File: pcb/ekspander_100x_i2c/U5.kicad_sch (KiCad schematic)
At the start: 12 parts, among them J12 DG127A-5.08-06P-14-00AH, J13 DG127A-5.08-06P-14-00AH, J14 DG127A-5.08-06P-14-00AH, U26 LTV-847, U27 ITS716G, U28 ITS716G, U29 LTV-847, U5 MCP23017_SP

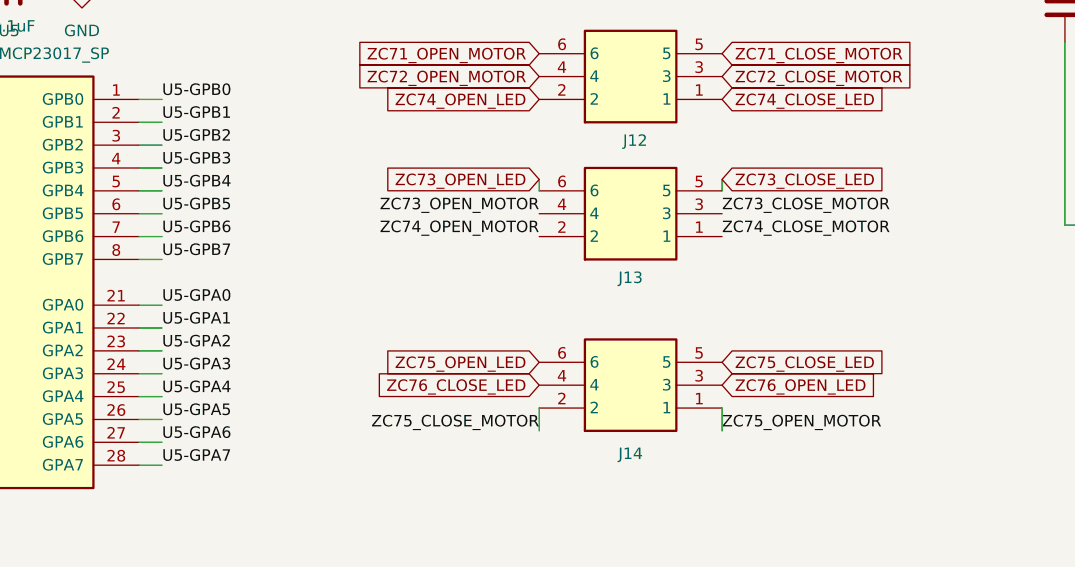
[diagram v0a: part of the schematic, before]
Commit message: Ekspander 100x - finish J
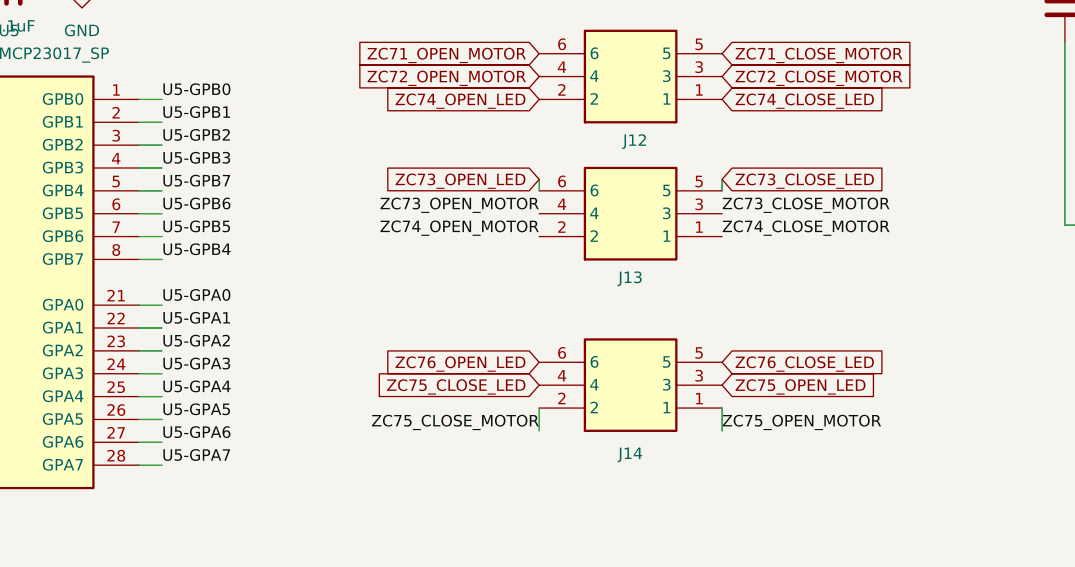
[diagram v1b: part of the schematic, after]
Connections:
- net U5-GPB4: now also U5.8 (GPB7); no longer U5.5 (GPB4)
- net U5-GPB5: now also U5.7 (GPB6); no longer U5.6 (GPB5)
- net U5-GPB6: now also U5.6 (GPB5); no longer U5.7 (GPB6)
- net U5-GPB7: now also U5.5 (GPB4); no longer U5.8 (GPB7)
- net ZC75_CLOSE_LED: now also J14.4; no longer J14.5
- net ZC75_OPEN_LED: now also J14.3; no longer J14.6
- net ZC76_CLOSE_LED: now also J14.5; no longer J14.4
- net ZC76_OPEN_LED: now also J14.6; no longer J14.3
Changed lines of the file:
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@@
 	)
 	(label "U5-GPB5"
-		(at 69.85 50.8 0)
-		(effects
-			(font
-				(size 1.27 1.27)
-			)
-			(justify left bottom)
-		)
-		(property "Netclass" "GPIO"
-			(at 79.756 50.8 0)
+		(at 69.85 53.34 0)
+		(effects
+			(font
+				(size 1.27 1.27)
+			)
+			(justify left bottom)
+		)
+		(property "Netclass" "GPIO"
+			(at 79.756 53.34 0)
 			(effects
 				(font
@@
 	)
 	(label "U5-GPB7"
-		(at 69.85 55.88 0)
-		(effects
-			(font
-				(size 1.27 1.27)
-			)
-			(justify left bottom)
-		)
-		(property "Netclass" "GPIO"
-			(at 79.756 55.88 0)
+		(at 69.85 48.26 0)
+		(effects
+			(font
+				(size 1.27 1.27)
+			)
+			(justify left bottom)
+		)
+		(property "Netclass" "GPIO"
+			(at 79.756 48.26 0)
 			(effects
 				(font
@@
 	)
 	(label "U5-GPB4"
-		(at 69.85 48.26 0)
-		(effects
-			(font
-				(size 1.27 1.27)
-			)
-			(justify left bottom)
-		)
-		(property "Netclass" "GPIO"
-			(at 80.01 48.26 0)
+		(at 69.85 55.88 0)
+		(effects
+			(font
+				(size 1.27 1.27)
+			)
+			(justify left bottom)
+		)
+		(property "Netclass" "GPIO"
+			(at 80.01 55.88 0)
 			(effects
 				(font
@@
 	)
 	(label "U5-GPB6"
-		(at 69.85 53.34 0)
-		(effects
-			(font
-				(size 1.27 1.27)
-			)
-			(justify left bottom)
-		)
-		(property "Netclass" "GPIO"
-			(at 79.756 53.34 0)
+		(at 69.85 50.8 0)
+		(effects
+			(font
+				(size 1.27 1.27)
+			)
+			(justify left bottom)
+		)
+		(property "Netclass" "GPIO"
+			(at 79.756 50.8 0)
 			(effects
 				(font
@@
 	(global_label "ZC76_CLOSE_LED"
 		(shape input)
-		(at 111.76 69.85 180)
-		(fields_autoplaced yes)
-		(effects
-			(font
-				(size 1.27 1.27)
-			)
-			(justify right)
-		)
-		(property "Intersheetrefs" "${INTERSHEET_REFS}"
-			(at 92.5069 69.85 0)
-			(effects
-				(font
-					(size 1.27 1.27)
-				)
-				(justify right)
+		(at 132.08 67.31 0)
+		(fields_autoplaced yes)
+		(effects
+			(font
+				(size 1.27 1.27)
+			)
+			(justify left)
+		)
+		(property "Intersheetrefs" "${INTERSHEET_REFS}"
+			(at 151.3331 67.31 0)
+			(effects
+				(font
+					(size 1.27 1.27)
+				)
+				(justify left)
 				(hide yes)
 			)
@@
 	(global_label "ZC75_OPEN_LED"
 		(shape input)
-		(at 111.76 67.31 180)
-		(fields_autoplaced yes)
-		(effects
-			(font
-				(size 1.27 1.27)
-			)
-			(justify right)
-		)
-		(property "Intersheetrefs" "${INTERSHEET_REFS}"
-			(at 93.414 67.31 0)
-			(effects
-				(font
-					(size 1.27 1.27)
-				)
-				(justify right)
+		(at 132.08 69.85 0)
+		(fields_autoplaced yes)
+		(effects
+			(font
+				(size 1.27 1.27)
+			)
+			(justify left)
+		)
+		(property "Intersheetrefs" "${INTERSHEET_REFS}"
+			(at 150.426 69.85 0)
+			(effects
+				(font
+					(size 1.27 1.27)
+				)
+				(justify left)
 				(hide yes)
 			)
@@
 	(global_label "ZC75_CLOSE_LED"
 		(shape input)
-		(at 132.08 67.31 0)
-		(fields_autoplaced yes)
-		(effects
-			(font
-				(size 1.27 1.27)
-			)
-			(justify left)
-		)
-		(property "Intersheetrefs" "${INTERSHEET_REFS}"
-			(at 151.3331 67.31 0)
-			(effects
-				(font
-					(size 1.27 1.27)
-				)
-				(justify left)
+		(at 111.76 69.85 180)
+		(fields_autoplaced yes)
+		(effects
+			(font
+				(size 1.27 1.27)
+			)
+			(justify right)
+		)
+		(property "Intersheetrefs" "${INTERSHEET_REFS}"
+			(at 92.5069 69.85 0)
+			(effects
+				(font
+					(size 1.27 1.27)
+				)
+				(justify right)
 				(hide yes)
 			)
@@
 	(global_label "ZC76_OPEN_LED"
 		(shape input)
-		(at 132.08 69.85 0)
-		(fields_autoplaced yes)
-		(effects
-			(font
-				(size 1.27 1.27)
-			)
-			(justify left)
-		)
-		(property "Intersheetrefs" "${INTERSHEET_REFS}"
-			(at 150.426 69.85 0)
-			(effects
-				(font
-					(size 1.27 1.27)
-				)
-				(justify left)
-				(hide yes)
-			)
+		(at 111.76 67.31 180)
+		(fields_autoplaced yes)
+		(effects
+			(font
+				(size 1.27 1.27)
+			)
+			(justify right)
+		)
+		(property "Intersheetrefs" "${INTERSHEET_REFS}"
+			(at 93.414 67.31 0)
+			(effects
+				(font
+					(size 1.27 1.27)
+				)
+				(justify right)
+				(hide yes)
+			)

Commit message: Tech Explorations
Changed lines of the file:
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@@
 		)
 		(property "Value" "+3V3"
-			(at 44.704 21.59 0)
+			(at 48.006 18.034 0)
 			(effects
 				(font
@@
 		(on_board yes)
 		(dnp no)
-		(fields_autoplaced yes)
 		(property "Reference" "R6"
-			(at 43.18 21.59 90)
+			(at 40.132 21.336 90)
 			(effects
 				(font
@@
 		(on_board yes)
 		(dnp no)
-		(fields_autoplaced yes)
 		(property "Reference" "U5"
-			(at 51.6733 30.48 0)
-			(effects
-				(font
+			(at 43.18 33.274 0)
+			(effects
+				(font

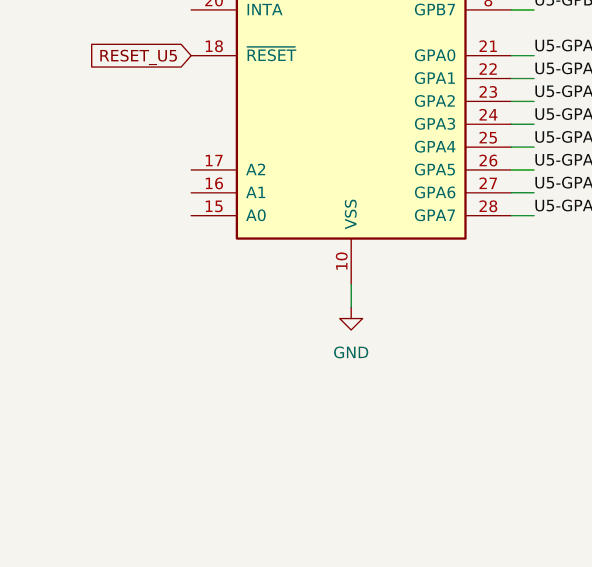
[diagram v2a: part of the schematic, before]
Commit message: Ekspander 100x - adresacja I2C - MCP23017
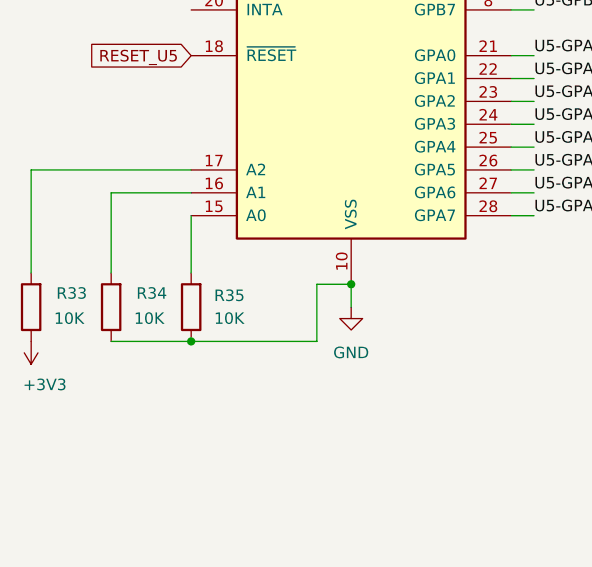
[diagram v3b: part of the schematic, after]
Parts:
- added R33, R34, R35: 10K, PCM_Resistor_SMD_AKL:R_0805_2012Metric_Pad1.20x1.40mm_HandSolder, symbol Device:R
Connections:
- net +3V3: now also R33.1
- net GND: now also R34.1, R35.1
- net at U5.15 (A0): now also R35.2
- net at U5.16 (A1): now also R34.2
- net at U5.17 (A2): now also R33.2

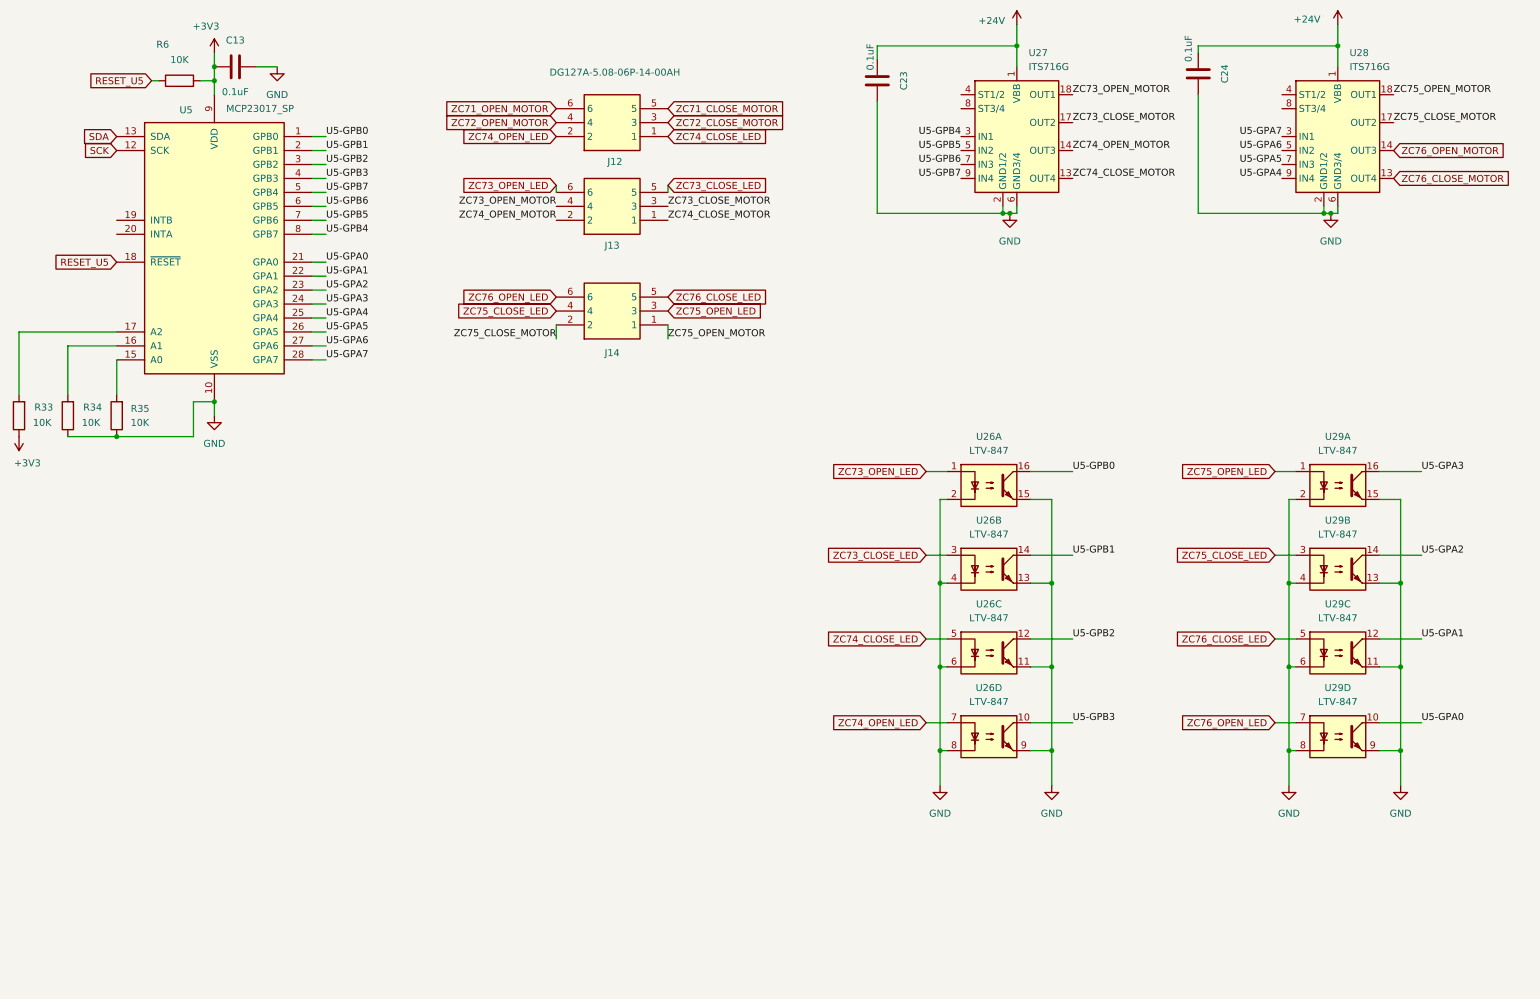
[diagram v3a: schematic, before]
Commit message: Ekspander 100x - diagnostic LEDs
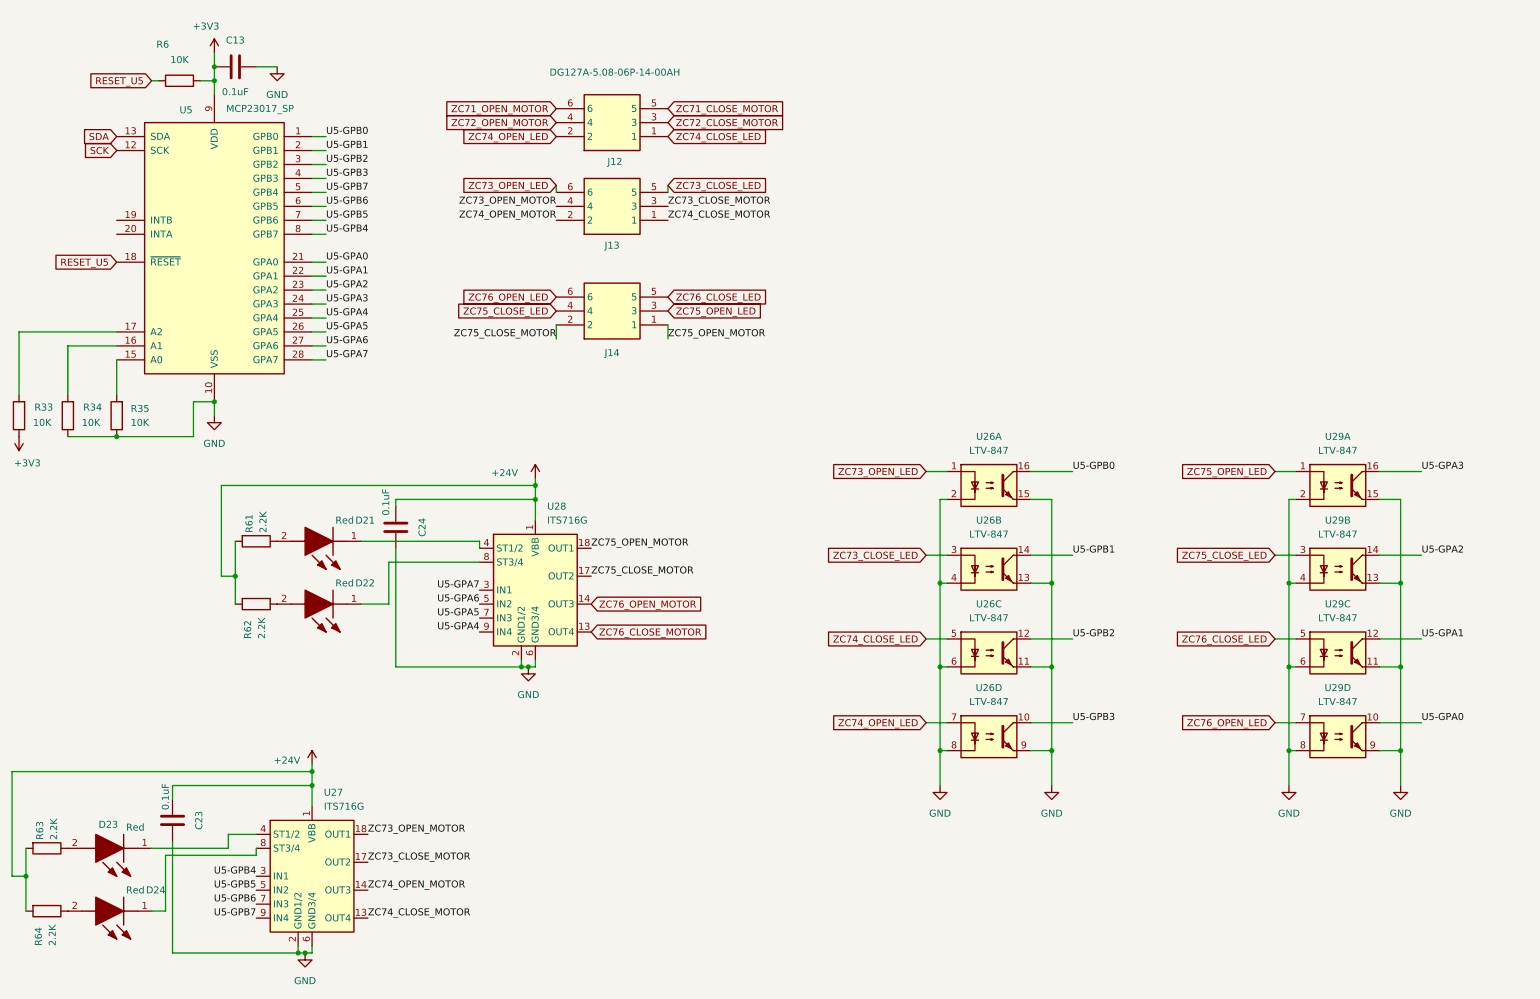
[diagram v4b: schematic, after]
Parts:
- added D21, D22, D23, D24: Red, 1_tme:LEDC2012X120N, symbol LTST-C170KRKT:LTST-C170KRKT
- added R61, R62, R63, R64: 2.2K, PCM_Resistor_SMD_AKL:R_0805_2012Metric_Pad1.20x1.40mm_HandSolder, symbol Device:R
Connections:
- net +24V: now also R61.2, R62.2, R63.2, R64.2
- net at U27.4 (ST1/2): now also D23.1 (K)
- net at U27.8 (ST3/4): now also D24.1 (K)
- net at U28.4 (ST1/2): now also D21.1 (K)
- net at U28.8 (ST3/4): now also D22.1 (K)
- new net: D22.2 (A), R62.1
- new net: D23.2 (A), R63.1
- new net: D21.2 (A), R61.1
- new net: D24.2 (A), R64.1
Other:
- moved on the sheet: C23, C24, U27, U28
